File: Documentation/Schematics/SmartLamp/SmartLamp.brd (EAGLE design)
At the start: 78.4 x 49.5 mm, 25 parts, among them J1 POWER_JACKPTH_BREAD, Q1 IRLZ44Z, Q2 IRLZ44Z, Q3 IRLZ44Z, U1 HM-10, U2 DS3231MZ

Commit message: Fixed 3.3V path in schematic
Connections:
- removed net 3V3: C2.1, IDC1.2, MCU1.1
- net +3V3: now also C2.1, IDC1.2, MCU1.1
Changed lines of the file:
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@@
 <wire x1="25.4" y1="11.43" x2="11.43" y2="17.78" width="0" layer="19" extent="1-1"/>
-</signal>
-<signal name="3V3" class="2">
-<contactref element="C2" pad="1"/>
-<contactref element="MCU1" pad="1"/>
-<contactref element="IDC1" pad="2"/>
-<wire x1="3.81" y1="30.48" x2="15.24" y2="24.13" width="0" layer="19" extent="1-1"/>
-<wire x1="22.86" y1="6.35" x2="15.24" y2="24.13" width="0" layer="19" extent="1-1"/>
 </signal>
 <signal name="!INT_SQW">
@@
 <contactref element="C4" pad="1"/>
 <contactref element="U1" pad="12"/>
+<contactref element="C2" pad="1"/>
+<contactref element="MCU1" pad="1"/>
+<contactref element="IDC1" pad="2"/>
 <wire x1="43.18" y1="12.7" x2="67.31" y2="26.67" width="0" layer="19" extent="1-1"/>
 <wire x1="38.1" y1="11.43" x2="43.18" y2="12.7" width="0" layer="19" extent="1-1"/>
@@
 <wire x1="25.39" y1="33.87" x2="29.21" y2="27.94" width="0" layer="19" extent="1-1"/>
 <wire x1="20.32" y1="24.13" x2="29.21" y2="27.94" width="0" layer="19" extent="1-1"/>
-<wire x1="15.3162" y1="29.845" x2="20.32" y2="24.13" width="0" layer="19" extent="1-1"/>
+<wire x1="15.24" y1="24.13" x2="20.32" y2="24.13" width="0" layer="19" extent="1-1"/>
+<wire x1="15.3162" y1="29.845" x2="15.24" y2="24.13" width="0" layer="19" extent="1-1"/>
 <wire x1="46.99" y1="2.7178" x2="43.18" y2="12.7" width="0" layer="19" extent="1-1"/>
+<wire x1="3.81" y1="30.48" x2="15.3162" y2="29.845" width="0" layer="19" extent="1-1"/>
+<wire x1="22.86" y1="6.35" x2="38.1" y2="11.43" width="0" layer="19" extent="1-1"/>
 </signal>
 <signal name="N$1">

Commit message: Added pullup on SQW pin
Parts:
- added R9: 10K, rcl:0309/12
- moved LED1 1.80 mm to (12.7, 2.54)
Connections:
- net !INT_SQW: now also R9.2
- net +3V3: now also R9.1
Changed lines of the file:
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@@
 <element name="C3" library="SparkFun-Capacitors" package="CPOL-RADIAL-10UF-25V" value="100uf" x="67.31" y="27.94" rot="R270"/>
 <element name="C4" library="adafruit" package="C025-024X044" value="0.1uF" x="29.21" y="29.21" rot="R90"/>
-<element name="LED1" library="adafruit" package="LED3MM" value="GREEN" x="13.97" y="3.81" rot="R90"/>
+<element name="LED1" library="adafruit" package="LED3MM" value="GREEN" x="12.7" y="2.54" rot="R90"/>
 <element name="LF33ABV" library="ST Microelctronics_By_element14_Batch_1" package="TO254P450X1020X1935-3P" value="LF33ABV" x="46.99" y="3.81">
 <attribute name="SUPPLIER" value="STMicroelectronics" x="46.99" y="3.81" size="1.778" layer="27" display="off"/>
@@
 <element name="Q2" library="transistor-power" package="TO220BH" value="IRLZ44Z" x="48.26" y="33.02"/>
 <element name="Q3" library="transistor-power" package="TO220BH" value="IRLZ44Z" x="36.83" y="33.02"/>
+<element name="R9" library="rcl" package="0309/12" value="10K" x="15.24" y="12.7" rot="R90"/>
 </elements>
 <signals>
@@
 <wire x1="28.96" y1="45.91" x2="28.96" y2="35.41" width="0" layer="19" extent="1-1"/>
 <wire x1="26.89" y1="47.41" x2="28.96" y2="45.91" width="0" layer="19" extent="1-1"/>
-<wire x1="13.97" y1="5.08" x2="15.24" y2="21.59" width="0" layer="19" extent="1-1"/>
-<wire x1="7.62" y1="2.54" x2="13.97" y2="5.08" width="0" layer="19" extent="1-1"/>
+<wire x1="72.04" y1="12.7" x2="62.23" y2="26.67" width="0" layer="19" extent="1-1"/>
+<wire x1="12.7" y1="3.81" x2="15.24" y2="21.59" width="0" layer="19" extent="1-1"/>
+<wire x1="7.62" y1="2.54" x2="12.7" y2="3.81" width="0" layer="19" extent="1-1"/>
 <wire x1="5.08" y1="2.54" x2="7.62" y2="2.54" width="0" layer="19" extent="1-1"/>
-<wire x1="30.48" y1="6.35" x2="13.97" y2="5.08" width="0" layer="19" extent="1-1"/>
+<wire x1="30.48" y1="6.35" x2="12.7" y2="3.81" width="0" layer="19" extent="1-1"/>
 <wire x1="33.02" y1="6.35" x2="30.48" y2="6.35" width="0" layer="19" extent="1-1"/>
 <wire x1="44.45" y1="2.7178" x2="33.02" y2="6.35" width="0" layer="19" extent="1-1"/>
-<wire x1="72.04" y1="12.7" x2="62.23" y2="26.67" width="0" layer="19" extent="1-1"/>
 </signal>
 <signal name="SDA">
@@
 <contactref element="U2" pad="3"/>
 <contactref element="MCU1" pad="13"/>
+<contactref element="R9" pad="2"/>
 <wire x1="11.43" y1="27.94" x2="15.3162" y2="28.575" width="0" layer="19" extent="1-1"/>
-<wire x1="30.48" y1="3.81" x2="15.3162" y2="28.575" width="0" layer="19" extent="1-1"/>
+<wire x1="15.24" y1="19.05" x2="15.3162" y2="28.575" width="0" layer="19" extent="1-1"/>
+<wire x1="30.48" y1="3.81" x2="15.24" y2="19.05" width="0" layer="19" extent="1-1"/>
 </signal>
 <signal name="RESET">
@@
 <contactref element="R8" pad="1"/>
 <contactref element="LED1" pad="A"/>
-<wire x1="13.97" y1="2.54" x2="25.4" y2="19.05" width="0" layer="19" extent="1-1"/>
+<wire x1="12.7" y1="1.27" x2="25.4" y2="19.05" width="0" layer="19" extent="1-1"/>
 </signal>
 <signal name="BLU_KEY">
@@
 <contactref element="MCU1" pad="1"/>
 <contactref element="IDC1" pad="2"/>
+<contactref element="R9" pad="1"/>
 <wire x1="43.18" y1="12.7" x2="67.31" y2="26.67" width="0" layer="19" extent="1-1"/>
 <wire x1="38.1" y1="11.43" x2="43.18" y2="12.7" width="0" layer="19" extent="1-1"/>
@@
 <wire x1="3.81" y1="30.48" x2="15.3162" y2="29.845" width="0" layer="19" extent="1-1"/>
 <wire x1="22.86" y1="6.35" x2="38.1" y2="11.43" width="0" layer="19" extent="1-1"/>
+<wire x1="15.24" y1="6.35" x2="22.86" y2="6.35" width="0" layer="19" extent="1-1"/>
 </signal>
 <signal name="N$1">

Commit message: Fixed input/output pins and synch with schematic. Added PCINT interrupt on INT_SQW line from RTC
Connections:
- net !BLU_RES: now also MCU1.2; no longer MCU1.12
- net BLU_STATE: now also MCU1.11; no longer MCU1.3
- net GR: now also MCU1.3; no longer MCU1.11
- net S_OUT_DEBUG: now also MCU1.12; no longer MCU1.2
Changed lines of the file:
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@@
 <contactref element="U1" pad="24"/>
 <contactref element="R8" pad="2"/>
-<contactref element="MCU1" pad="3"/>
-<wire x1="3.81" y1="25.4" x2="23.89" y2="47.41" width="0" layer="19" extent="1-1"/>
-<wire x1="38.1" y1="19.05" x2="23.89" y2="47.41" width="0" layer="19" extent="1-1"/>
+<contactref element="MCU1" pad="11"/>
+<wire x1="11.43" y1="22.86" x2="23.89" y2="47.41" width="0" layer="19" extent="1-1"/>
+<wire x1="38.1" y1="19.05" x2="11.43" y2="22.86" width="0" layer="19" extent="1-1"/>
 </signal>
 <signal name="N$10">
@@
 <contactref element="R4" pad="1"/>
 <contactref element="IDC1" pad="1"/>
-<contactref element="MCU1" pad="11"/>
+<contactref element="MCU1" pad="3"/>
 <wire x1="22.86" y1="3.81" x2="40.64" y2="12.7" width="0" layer="19" extent="1-1"/>
-<wire x1="11.43" y1="22.86" x2="22.86" y2="3.81" width="0" layer="19" extent="1-1"/>
+<wire x1="3.81" y1="25.4" x2="22.86" y2="3.81" width="0" layer="19" extent="1-1"/>
 </signal>
 <signal name="BLUE">
@@
 <signal name="!BLU_RES">
 <contactref element="U1" pad="11"/>
-<contactref element="MCU1" pad="12"/>
-<wire x1="11.43" y1="25.4" x2="23.89" y2="33.87" width="0" layer="19" extent="1-1"/>
+<contactref element="MCU1" pad="2"/>
+<wire x1="3.81" y1="27.94" x2="23.89" y2="33.87" width="0" layer="19" extent="1-1"/>
 </signal>
 <signal name="VBAT">
@@
 <signal name="S_OUT_DEBUG">
 <contactref element="IDC1" pad="6"/>
-<contactref element="MCU1" pad="2"/>
-<wire x1="3.81" y1="27.94" x2="27.94" y2="6.35" width="0" layer="19" extent="1-1"/>
+<contactref element="MCU1" pad="12"/>
+<wire x1="27.94" y1="6.35" x2="11.43" y2="25.4" width="0" layer="19" extent="1-1"/>
 </signal>
 <signal name="+3V3" class="2">

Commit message: Removed SoftwareSerial library! Used CORE Serial instead. Fixed ISR(PCINT0_vect) call, enable PCINT0 and PCINT2 interrupt. Reviewed input/output pins.
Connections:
- removed net S_OUT_DEBUG: IDC1.6, MCU1.12
- net BLU_STATE: now also MCU1.6; no longer MCU1.11
- net S_IN: now also MCU1.11; no longer MCU1.5
- net S_OUT: now also IDC1.6, MCU1.12; no longer MCU1.6
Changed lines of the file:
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@@
 </signal>
 <signal name="S_OUT">
-<contactref element="MCU1" pad="6"/>
 <contactref element="U1" pad="2"/>
-<wire x1="3.81" y1="17.78" x2="10.39" y2="33.87" width="0" layer="19" extent="1-1"/>
+<contactref element="IDC1" pad="6"/>
+<contactref element="MCU1" pad="12"/>
+<wire x1="11.43" y1="25.4" x2="10.39" y2="33.87" width="0" layer="19" extent="1-1"/>
+<wire x1="27.94" y1="6.35" x2="11.43" y2="25.4" width="0" layer="19" extent="1-1"/>
 </signal>
 <signal name="S_IN">
-<contactref element="MCU1" pad="5"/>
 <contactref element="U1" pad="1"/>
-<wire x1="3.81" y1="20.32" x2="8.89" y2="33.87" width="0" layer="19" extent="1-1"/>
+<contactref element="MCU1" pad="11"/>
+<wire x1="11.43" y1="22.86" x2="8.89" y2="33.87" width="0" layer="19" extent="1-1"/>
 </signal>
 <signal name="BLU_STATE">
 <contactref element="U1" pad="24"/>
 <contactref element="R8" pad="2"/>
-<contactref element="MCU1" pad="11"/>
-<wire x1="11.43" y1="22.86" x2="23.89" y2="47.41" width="0" layer="19" extent="1-1"/>
-<wire x1="38.1" y1="19.05" x2="11.43" y2="22.86" width="0" layer="19" extent="1-1"/>
+<contactref element="MCU1" pad="6"/>
+<wire x1="38.1" y1="19.05" x2="23.89" y2="47.41" width="0" layer="19" extent="1-1"/>
+<wire x1="3.81" y1="17.78" x2="38.1" y2="19.05" width="0" layer="19" extent="1-1"/>
 </signal>
 <signal name="N$10">
@@
 <wire x1="20.2438" y1="28.575" x2="52.04" y2="12.7" width="0" layer="19" extent="1-1"/>
 </signal>
-<signal name="S_OUT_DEBUG">
-<contactref element="IDC1" pad="6"/>
-<contactref element="MCU1" pad="12"/>
-<wire x1="27.94" y1="6.35" x2="11.43" y2="25.4" width="0" layer="19" extent="1-1"/>
-</signal>
 <signal name="+3V3" class="2">

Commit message: Fixed output pins to use PWM... ops. Added PWM test cycle.
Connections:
- net BLU_STATE: now also MCU1.3; no longer MCU1.6
- net GR: now also MCU1.6; no longer MCU1.3
- net RED: now also MCU1.5; no longer MCU1.10
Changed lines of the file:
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@@
 <contactref element="U1" pad="24"/>
 <contactref element="R8" pad="2"/>
-<contactref element="MCU1" pad="6"/>
+<contactref element="MCU1" pad="3"/>
+<wire x1="3.81" y1="25.4" x2="23.89" y2="47.41" width="0" layer="19" extent="1-1"/>
 <wire x1="38.1" y1="19.05" x2="23.89" y2="47.41" width="0" layer="19" extent="1-1"/>
-<wire x1="3.81" y1="17.78" x2="38.1" y2="19.05" width="0" layer="19" extent="1-1"/>
 </signal>
 <signal name="N$10">
@@
 <signal name="RED">
 <contactref element="R3" pad="1"/>
-<contactref element="MCU1" pad="10"/>
-<wire x1="11.43" y1="20.32" x2="45.72" y2="12.7" width="0" layer="19" extent="1-1"/>
+<contactref element="MCU1" pad="5"/>
+<wire x1="3.81" y1="20.32" x2="45.72" y2="12.7" width="0" layer="19" extent="1-1"/>
 </signal>
 <signal name="GR">
 <contactref element="R4" pad="1"/>
 <contactref element="IDC1" pad="1"/>
-<contactref element="MCU1" pad="3"/>
+<contactref element="MCU1" pad="6"/>
 <wire x1="22.86" y1="3.81" x2="40.64" y2="12.7" width="0" layer="19" extent="1-1"/>
-<wire x1="3.81" y1="25.4" x2="22.86" y2="3.81" width="0" layer="19" extent="1-1"/>
+<wire x1="3.81" y1="17.78" x2="22.86" y2="3.81" width="0" layer="19" extent="1-1"/>
 </signal>
 <signal name="BLUE">

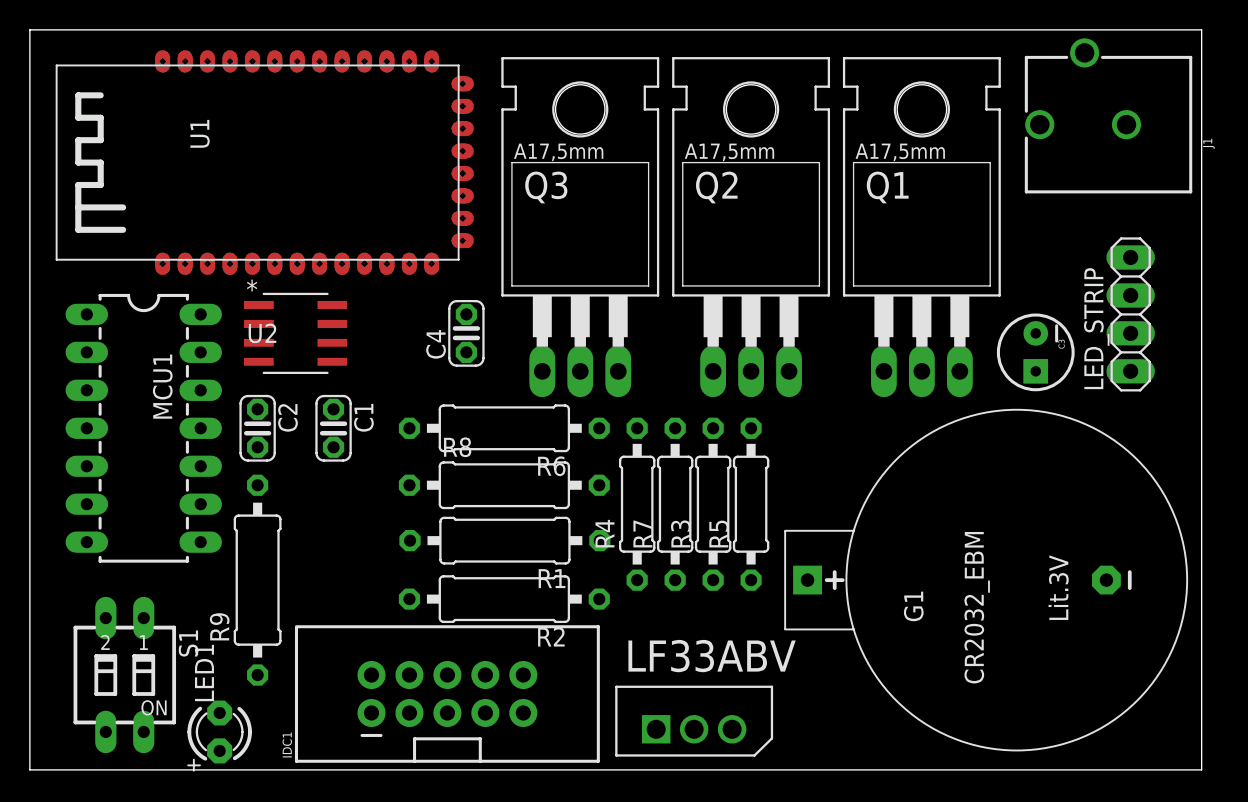
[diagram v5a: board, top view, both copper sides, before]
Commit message: Fixed IDC connection (ISP programmer). Completed routing, added ground and signal plane.
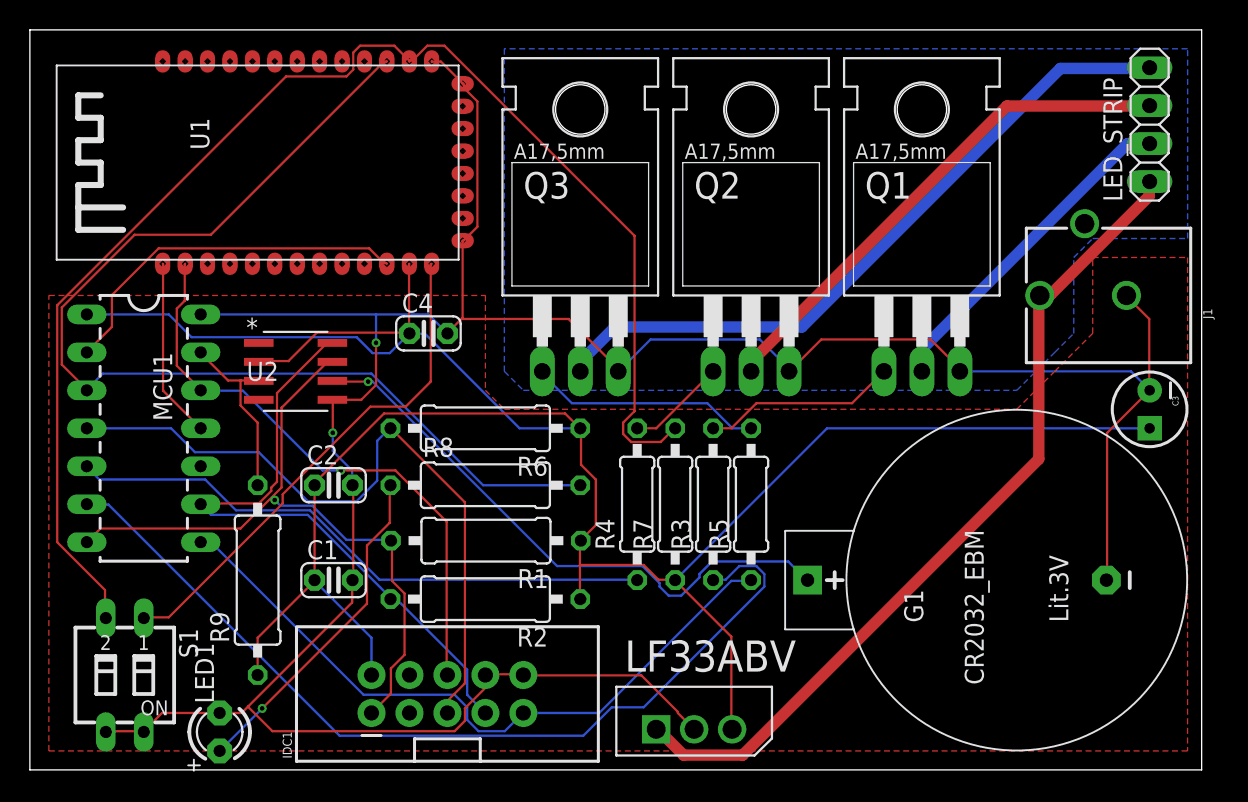
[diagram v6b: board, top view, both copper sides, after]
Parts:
- moved LED_STRIP 12.8 mm to (74.9, 43.2)
- moved J1 11.4 mm to (81.3, 31.8)
- moved C1 10.2 mm to (20.3, 12.7), turned to 0 degrees
- moved C3 8.52 mm to (74.9, 24.1)
- moved C2 6.35 mm to (20.3, 19.1), turned to 0 degrees
- moved C4 2.54 mm to (26.7, 29.2), turned to 0 degrees
- moved U2 2.54 mm to (17.8, 26.7)
- moved R1 1.27 mm to (30.5, 15.3)
- moved R2 1.27 mm to (30.5, 11.4)
- moved R6 1.27 mm to (30.5, 22.9)
- moved R8 1.27 mm to (30.5, 19.1)
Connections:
- net N$1 renamed BLU_SWITCH
- net N$3 renamed GR_12V
- net N$4 renamed RED_12V
- net N$6 renamed BLUE_12V
- net !INT_SQW: no longer IDC1.7
- net GR: now also R3.1; no longer IDC1.1, R4.1
- net RED: now also R4.1; no longer R3.1
- net SCL: now also IDC1.7
- net SDA: now also IDC1.1
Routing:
- net GND: track 0.00 -> 187.7 mm, vias 0 -> 2
- net +3V3: track 0.00 -> 162.0 mm
- net BLU_KEY: track 0.00 -> 92.6 mm
- net BLU_STATE: track 0.00 -> 71.4 mm
- net GR: track 0.00 -> 60.8 mm
- net +12V: track 0.00 -> 56.6 mm
- net RESET: track 0.00 -> 47.5 mm
- net BLUE_12V: track 0.00 -> 46.9 mm
- net BLUE: track 0.00 -> 46.8 mm
- net SDA: track 0.00 -> 46.6 mm, vias 0 -> 1
- net SCL: track 0.00 -> 42.9 mm
- net RED: track 0.00 -> 40.0 mm
- net S_OUT: track 0.00 -> 39.8 mm, vias 0 -> 1
- net VBAT: track 0.00 -> 39.5 mm, vias 0 -> 1
- net RED_12V: track 0.00 -> 34.4 mm
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- added copper zone on layer 16, net +12V
- added copper zone on layer 1, net GND
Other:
- board text added: "SmartLamp v1.0"
